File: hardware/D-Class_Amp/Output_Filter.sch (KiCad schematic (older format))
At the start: 4 parts

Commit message: single side
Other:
- moved on the sheet: C?, L?
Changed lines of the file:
@@
 Comment4 ""
 $EndDescr
-Text HLabel 1450 1200 0    50   Input ~ 0
+Text HLabel 3700 3500 0    50   Input ~ 0
 SIG_IN
-Text HLabel 1450 2050 0    50   Input ~ 0
+Text HLabel 7650 3500 2    50   Input ~ 0
 ~SIG_IN
 $Comp
 L Device:L L?
 U 1 1 61193FAD
-P 1850 1200
-F 0 "L?" V 2040 1200 50  0000 C CNN
-F 1 "L" V 1949 1200 50  0000 C CNN
-F 2 "" H 1850 1200 50  0001 C CNN
-F 3 "~" H 1850 1200 50  0001 C CNN
-	1    1850 1200
+P 4100 3500
+F 0 "L?" V 4290 3500 50  0000 C CNN
+F 1 "L" V 4199 3500 50  0000 C CNN
+F 2 "" H 4100 3500 50  0001 C CNN
+F 3 "~" H 4100 3500 50  0001 C CNN
+	1    4100 3500
 	0    -1   -1   0
 $EndComp
@@
 L Device:L L?
 U 1 1 61195264
-P 1850 2050
-F 0 "L?" V 2040 2050 50  0000 C CNN
-F 1 "L" V 1949 2050 50  0000 C CNN
-F 2 "" H 1850 2050 50  0001 C CNN
-F 3 "~" H 1850 2050 50  0001 C CNN
-	1    1850 2050
-	0    -1   -1   0
+P 7250 3500
+F 0 "L?" V 7440 3500 50  0000 C CNN
+F 1 "L" V 7349 3500 50  0000 C CNN
+F 2 "" H 7250 3500 50  0001 C CNN
+F 3 "~" H 7250 3500 50  0001 C CNN
+	1    7250 3500
+	0    1    -1   0
 $EndComp
 $Comp
 L Device:C C?
 U 1 1 611955B4
-P 2350 1400
-F 0 "C?" H 2465 1446 50  0000 L CNN
-F 1 "C" H 2465 1355 50  0000 L CNN
-F 2 "" H 2388 1250 50  0001 C CNN
-F 3 "~" H 2350 1400 50  0001 C CNN
-	1    2350 1400
+P 4600 3700
+F 0 "C?" H 4715 3746 50  0000 L CNN
+F 1 "C" H 4715 3655 50  0000 L CNN
+F 2 "" H 4638 3550 50  0001 C CNN
+F 3 "~" H 4600 3700 50  0001 C CNN
+	1    4600 3700
 	1    0    0    -1
 $EndComp
@@
 L Device:C C?
 U 1 1 61195DF7
-P 2350 2250
-F 0 "C?" H 2465 2296 50  0000 L CNN
-F 1 "C" H 2465 2205 50  0000 L CNN
-F 2 "" H 2388 2100 50  0001 C CNN
-F 3 "~" H 2350 2250 50  0001 C CNN
-	1    2350 2250
-	1    0    0    -1
+P 6750 3700
+F 0 "C?" H 6865 3746 50  0000 L CNN
+F 1 "C" H 6865 3655 50  0000 L CNN
+F 2 "" H 6788 3550 50  0001 C CNN
+F 3 "~" H 6750 3700 50  0001 C CNN
+	1    6750 3700
+	-1   0    0    -1
 $EndComp
 Wire Wire Line
-	1450 1200 1700 1200
+	3700 3500 3950 3500
 Wire Wire Line
-	2000 1200 2350 1200
+	4250 3500 4600 3500
 Wire Wire Line
-	2350 1200 2350 1250
+	4600 3500 4600 3550
 Wire Wire Line
-	2350 1200 2700 1200
-Connection ~ 2350 1200
+	4600 3500 4950 3500
+Connection ~ 4600 3500
 Wire Wire Line
-	1450 2050 1700 2050
+	7650 3500 7400 3500
 Wire Wire Line
-	2000 2050 2350 2050
+	7100 3500 6750 3500
 Wire Wire Line
-	2350 2050 2350 2100
+	6750 3500 6750 3550
 Wire Wire Line
-	2350 2050 2700 2050
-Connection ~ 2350 2050
+	6750 3500 6400 3500
+Connection ~ 6750 3500
 $Comp
 L power:GND #PWR?
 U 1 1 611D879A
-P 2350 1625
-F 0 "#PWR?" H 2350 1375 50  0001 C CNN
-F 1 "GND" H 2355 1452 50  0000 C CNN
-F 2 "" H 2350 1625 50  0001 C CNN
-F 3 "" H 2350 1625 50  0001 C CNN
-	1    2350 1625
+P 4600 3925
+F 0 "#PWR?" H 4600 3675 50  0001 C CNN
+F 1 "GND" H 4605 3752 50  0000 C CNN
+F 2 "" H 4600 3925 50  0001 C CNN
+F 3 "" H 4600 3925 50  0001 C CNN
+	1    4600 3925
 	1    0    0    -1
 $EndComp
@@
 L power:GND #PWR?
 U 1 1 611D8B24
-P 2350 2475
-F 0 "#PWR?" H 2350 2225 50  0001 C CNN
-F 1 "GND" H 2355 2302 50  0000 C CNN
-F 2 "" H 2350 2475 50  0001 C CNN
-F 3 "" H 2350 2475 50  0001 C CNN
-	1    2350 2475
-	1    0    0    -1
+P 6750 3925
+F 0 "#PWR?" H 6750 3675 50  0001 C CNN
+F 1 "GND" H 6755 3752 50  0000 C CNN
+F 2 "" H 6750 3925 50  0001 C CNN
+F 3 "" H 6750 3925 50  0001 C CNN
+	1    6750 3925
+	-1   0    0    -1
 $EndComp
 Wire Wire Line
-	2350 2475 2350 2400
+	6750 3925 6750 3850
 Wire Wire Line
-	2350 1625 2350 1550
-Text HLabel 2700 1200 2    50   Output ~ 0
+	4600 3925 4600 3850
+Text HLabel 4950 3500 2    50   Output ~ 0
 SPEAKER_OUT
-Text HLabel 2700 2050 2    50   Output ~ 0
+Text HLabel 6400 3500 0    50   Output ~ 0
 ~SPEAKER_OUT
 $EndSCHEMATC

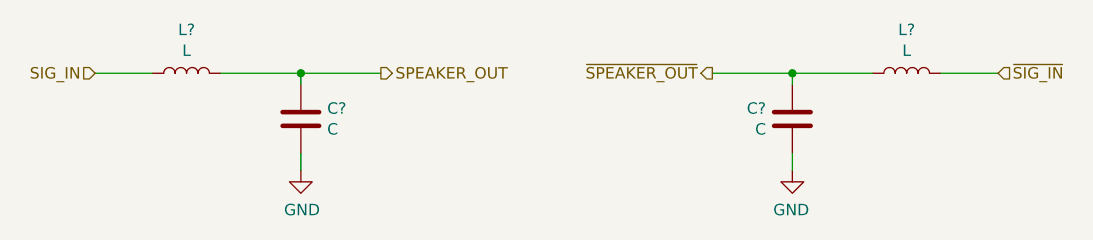
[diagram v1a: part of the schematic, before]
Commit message: Added input bias circuit and gain stage to input-stage schematic.
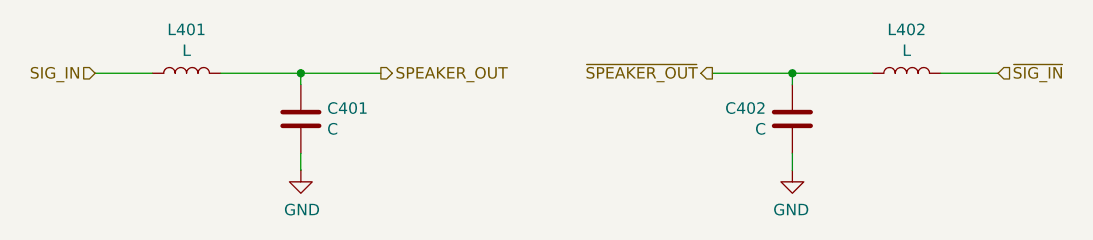
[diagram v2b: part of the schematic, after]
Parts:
- gave numbers to parts that had none: 4
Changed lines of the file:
@@
 ~SIG_IN
 $Comp
-L Device:L L?
+L Device:L L401
 U 1 1 61193FAD
 P 4100 3500
-F 0 "L?" V 4290 3500 50  0000 C CNN
+F 0 "L401" V 4290 3500 50  0000 C CNN
 F 1 "L" V 4199 3500 50  0000 C CNN
 F 2 "" H 4100 3500 50  0001 C CNN
@@
 $EndComp
 $Comp
-L Device:L L?
+L Device:L L402
 U 1 1 61195264
 P 7250 3500
-F 0 "L?" V 7440 3500 50  0000 C CNN
+F 0 "L402" V 7440 3500 50  0000 C CNN
 F 1 "L" V 7349 3500 50  0000 C CNN
 F 2 "" H 7250 3500 50  0001 C CNN
@@
 $EndComp
 $Comp
-L Device:C C?
+L Device:C C401
 U 1 1 611955B4
 P 4600 3700
-F 0 "C?" H 4715 3746 50  0000 L CNN
+F 0 "C401" H 4715 3746 50  0000 L CNN
 F 1 "C" H 4715 3655 50  0000 L CNN
 F 2 "" H 4638 3550 50  0001 C CNN
@@
 $EndComp
 $Comp
-L Device:C C?
+L Device:C C402
 U 1 1 61195DF7
 P 6750 3700
-F 0 "C?" H 6865 3746 50  0000 L CNN
+F 0 "C402" H 6865 3746 50  0000 L CNN
 F 1 "C" H 6865 3655 50  0000 L CNN
 F 2 "" H 6788 3550 50  0001 C CNN
@@
 Connection ~ 6750 3500
 $Comp
-L power:GND #PWR?
+L power:GND #PWR0401
 U 1 1 611D879A
 P 4600 3925
-F 0 "#PWR?" H 4600 3675 50  0001 C CNN
+F 0 "#PWR0401" H 4600 3675 50  0001 C CNN
 F 1 "GND" H 4605 3752 50  0000 C CNN
 F 2 "" H 4600 3925 50  0001 C CNN
@@
 $EndComp
 $Comp
-L power:GND #PWR?
+L power:GND #PWR0402
 U 1 1 611D8B24
 P 6750 3925
-F 0 "#PWR?" H 6750 3675 50  0001 C CNN
+F 0 "#PWR0402" H 6750 3675 50  0001 C CNN
 F 1 "GND" H 6755 3752 50  0000 C CNN
 F 2 "" H 6750 3925 50  0001 C CNN

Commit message: fixed remerge
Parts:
- added C?: 9.38u, symbol Device:C
- C401, C402: value C -> 1.88u
- L401, L402: value L -> 150u
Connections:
- net SPEAKER_OUT: now also C?.1
- net ~SIG_IN: now also L402.2; no longer L402.1
- net ~SPEAKER_OUT: now also L402.1, C?.2; no longer L402.2
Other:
- moved on the sheet: C401, C402, L401, L402
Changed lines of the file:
@@
 $Descr A4 11693 8268
 encoding utf-8
-Sheet 4 5
+Sheet 1 1
 Title ""
 Date ""
@@
 Comment4 ""
 $EndDescr
-Text HLabel 3700 3500 0    50   Input ~ 0
+Text HLabel 8375 4900 0    50   Input ~ 0
 SIG_IN
-Text HLabel 7650 3500 2    50   Input ~ 0
+Text HLabel 8375 5675 0    50   Input ~ 0
 ~SIG_IN
 $Comp
 L Device:L L401
 U 1 1 61193FAD
-P 4100 3500
-F 0 "L401" V 4290 3500 50  0000 C CNN
-F 1 "L" V 4199 3500 50  0000 C CNN
-F 2 "" H 4100 3500 50  0001 C CNN
-F 3 "~" H 4100 3500 50  0001 C CNN
-	1    4100 3500
+P 8675 4900
+F 0 "L401" V 8865 4900 50  0000 C CNN
+F 1 "150u" V 8774 4900 50  0000 C CNN
+F 2 "" H 8675 4900 50  0001 C CNN
+F 3 "~" H 8675 4900 50  0001 C CNN
+	1    8675 4900
 	0    -1   -1   0
 $EndComp
@@
 L Device:L L402
 U 1 1 61195264
-P 7250 3500
-F 0 "L402" V 7440 3500 50  0000 C CNN
-F 1 "L" V 7349 3500 50  0000 C CNN
-F 2 "" H 7250 3500 50  0001 C CNN
-F 3 "~" H 7250 3500 50  0001 C CNN
-	1    7250 3500
+P 8675 5675
+F 0 "L402" V 8865 5675 50  0000 C CNN
+F 1 "150u" V 8774 5675 50  0000 C CNN
+F 2 "" H 8675 5675 50  0001 C CNN
+F 3 "~" H 8675 5675 50  0001 C CNN
+	1    8675 5675
 	0    1    -1   0
 $EndComp
@@
 L Device:C C401
 U 1 1 611955B4
-P 4600 3700
-F 0 "C401" H 4715 3746 50  0000 L CNN
-F 1 "C" H 4715 3655 50  0000 L CNN
-F 2 "" H 4638 3550 50  0001 C CNN
-F 3 "~" H 4600 3700 50  0001 C CNN
-	1    4600 3700
+P 9175 5100
+F 0 "C401" H 9290 5146 50  0000 L CNN
+F 1 "1.88u" H 9290 5055 50  0000 L CNN
+F 2 "" H 9213 4950 50  0001 C CNN
+F 3 "~" H 9175 5100 50  0001 C CNN
+	1    9175 5100
 	1    0    0    -1
 $EndComp
@@
 L Device:C C402
 U 1 1 61195DF7
-P 6750 3700
-F 0 "C402" H 6865 3746 50  0000 L CNN
-F 1 "C" H 6865 3655 50  0000 L CNN
-F 2 "" H 6788 3550 50  0001 C CNN
-F 3 "~" H 6750 3700 50  0001 C CNN
-	1    6750 3700
-	-1   0    0    -1
+P 9175 5450
+F 0 "C402" H 9290 5496 50  0000 L CNN
+F 1 "1.88u" H 9290 5405 50  0000 L CNN
+F 2 "" H 9213 5300 50  0001 C CNN
+F 3 "~" H 9175 5450 50  0001 C CNN
+	1    9175 5450
+	1    0    0    1
 $EndComp
 Wire Wire Line
-	3700 3500 3950 3500
+	8375 4900 8525 4900
 Wire Wire Line
-	4250 3500 4600 3500
+	8825 4900 9175 4900
 Wire Wire Line
-	4600 3500 4600 3550
+	9175 4900 9175 4950
 Wire Wire Line
-	4600 3500 4950 3500
-Connection ~ 4600 3500
+	9175 4900 9575 4900
+Connection ~ 9175 4900
 Wire Wire Line
-	7650 3500 7400 3500
+	8375 5675 8525 5675
 Wire Wire Line
-	7100 3500 6750 3500
+	8825 5675 9175 5675
 Wire Wire Line
-	6750 3500 6750 3550
+	9175 5675 9175 5600
 Wire Wire Line
-	6750 3500 6400 3500
-Connection ~ 6750 3500
+	9175 5675 9575 5675
+Connection ~ 9175 5675
 $Comp
 L power:GND #PWR0401
 U 1 1 611D879A
-P 4600 3925
-F 0 "#PWR0401" H 4600 3675 50  0001 C CNN
-F 1 "GND" H 4605 3752 50  0000 C CNN
-F 2 "" H 4600 3925 50  0001 C CNN
-F 3 "" H 4600 3925 50  0001 C CNN
-	1    4600 3925
+P 8975 5350
+F 0 "#PWR0401" H 8975 5100 50  0001 C CNN
+F 1 "GND" H 8980 5177 50  0000 C CNN
+F 2 "" H 8975 5350 50  0001 C CNN
+F 3 "" H 8975 5350 50  0001 C CNN
+	1    8975 5350
 	1    0    0    -1
 $EndComp
+Wire Wire Line
+	9175 5300 9175 5275
+Text HLabel 9875 4900 2    50   Output ~ 0
+SPEAKER_OUT
+Text HLabel 9875 5675 2    50   Output ~ 0
+~SPEAKER_OUT
+Wire Wire Line
+	9175 5275 8975 5275
+Wire Wire Line
+	8975 5275 8975 5350
+Connection ~ 9175 5275
+Wire Wire Line
+	9175 5275 9175 5250
+Connection ~ 9575 5675
+Wire Wire Line
+	9575 5675 9875 5675
+Connection ~ 9575 4900
+Wire Wire Line
+	9575 4900 9875 4900
+Wire Wire Line
+	9575 5425 9575 5675
+Wire Wire Line
+	9575 5125 9575 4900
 $Comp
-L power:GND #PWR0402
-U 1 1 611D8B24
-P 6750 3925
-F 0 "#PWR0402" H 6750 3675 50  0001 C CNN
-F 1 "GND" H 6755 3752 50  0000 C CNN
-F 2 "" H 6750 3925 50  0001 C CNN
-F 3 "" H 6750 3925 50  0001 C CNN
-	1    6750 3925
-	-1   0    0    -1
+L Device:C C?
+U 1 1 611BA813
+P 9575 5275
+F 0 "C?" H 9690 5321 50  0000 L CNN
+F 1 "9.38u" H 9690 5230 50  0000 L CNN
+F 2 "" H 9613 5125 50  0001 C CNN
+F 3 "~" H 9575 5275 50  0001 C CNN
+	1    9575 5275
+	1    0    0    -1
 $EndComp
-Wire Wire Line
-	6750 3925 6750 3850
-Wire Wire Line
-	4600 3925 4600 3850
-Text HLabel 4950 3500 2    50   Output ~ 0
-SPEAKER_OUT
-Text HLabel 6400 3500 0    50   Output ~ 0
-~SPEAKER_OUT
 $EndSCHEMATC
